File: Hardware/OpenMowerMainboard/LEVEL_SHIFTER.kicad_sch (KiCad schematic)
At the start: 3 parts, among them Q16 BSS138

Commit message: BOM changes
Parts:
- Q16: Digikey (none) -> BSS138K-13DICT-ND
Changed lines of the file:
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@@
+      (effects (font (size 1.27 1.27)) hide)
+    )
+    (property "Digikey" "BSS138K-13DICT-ND" (id 7) (at 114.3 76.2 0)
       (effects (font (size 1.27 1.27)) hide)
     )

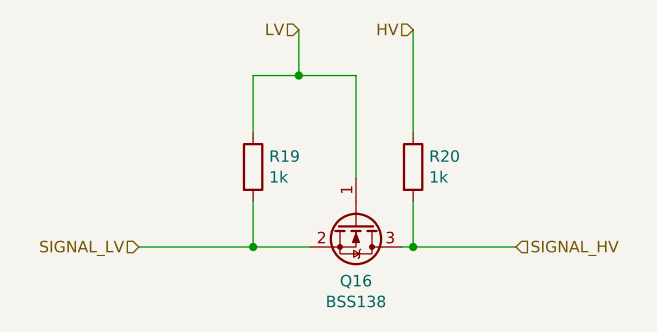
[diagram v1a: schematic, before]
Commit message: chore: save schematics and update PCB to sync in-line changes
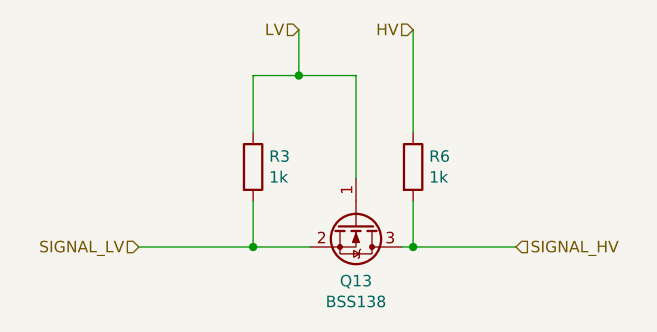
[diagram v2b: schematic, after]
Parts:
- renumbered Q16 to Q13, R19 to R3, R20 to R6
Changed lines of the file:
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@@
     (effects (font (size 1.27 1.27)) (justify right))
   )
-  (symbol (lib_id "Transistor_FET:BSS138") (at 114.3 76.2 270)
+  (symbol (lib_id "Transistor_FET:BSS138") (at 114.3 76.2 270) (unit 1)
     (in_bom yes) (on_board yes)
-    (property "Reference" "Q16" (id 0) (at 114.3 82.5246 90))
+    (property "Reference" "Q13" (id 0) (at 114.3 82.5246 90))
     (property "Value" "BSS138" (id 1) (at 114.3 84.836 90))
     (property "Footprint" "Package_TO_SOT_SMD:SOT-23" (id 2) (at 112.395 81.28 0)
@@
     (pin "3")
   )
-  (symbol (lib_id "Device:R") (at 102.87 69.85 0)
+  (symbol (lib_id "Device:R") (at 102.87 69.85 0) (unit 1)
     (in_bom yes) (on_board yes)
-    (property "Reference" "R19" (id 0) (at 104.648 68.6816 0)
+    (property "Reference" "R3" (id 0) (at 104.648 68.6816 0)
       (effects (font (size 1.27 1.27)) (justify left))
     )
@@
     (pin "2")
   )
-  (symbol (lib_id "Device:R") (at 120.65 69.85 0)
+  (symbol (lib_id "Device:R") (at 120.65 69.85 0) (unit 1)
     (in_bom yes) (on_board yes)
-    (property "Reference" "R20" (id 0) (at 122.428 68.6816 0)
+    (property "Reference" "R6" (id 0) (at 122.428 68.6816 0)
       (effects (font (size 1.27 1.27)) (justify left))
     )

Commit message: feat(bom): update LCSC codes
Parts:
- Q13: LCSC C360338 -> C3040446
- R3, R6: LCSC (none) -> C95781
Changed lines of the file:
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@@
       (effects (font (size 1.27 1.27)) (justify left) hide)
     )
-    (property "LCSC" "C360338" (id 4) (at 114.3 76.2 0)
+    (property "LCSC" "C3040446" (id 4) (at 114.3 76.2 0)
       (effects (font (size 1.27 1.27)) hide)
     )
@@
       (effects (font (size 1.27 1.27)) hide)
     )
+    (property "LCSC" "C95781" (id 7) (at 102.87 69.85 0)
+      (effects (font (size 1.27 1.27)) hide)
+    )
     (pin "1")
     (pin "2")
@@
       (effects (font (size 1.27 1.27)) hide)
     )
+    (property "LCSC" "C95781" (id 7) (at 120.65 69.85 0)
+      (effects (font (size 1.27 1.27)) hide)
+    )
